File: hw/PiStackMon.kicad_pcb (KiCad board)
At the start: 2 copper layers, 67.5 x 21.5 mm, 61 parts, among them J1 Conn_01x03, J10 Conn_01x02, J2 Conn_01x03, J3 Screw_Terminal_01x02, J4 Screw_Terminal_01x02, J5 Conn_01x02, J6 Conn_01x02, J7 Conn_01x07, J8 Conn_01x05, J9 Conn_01x03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

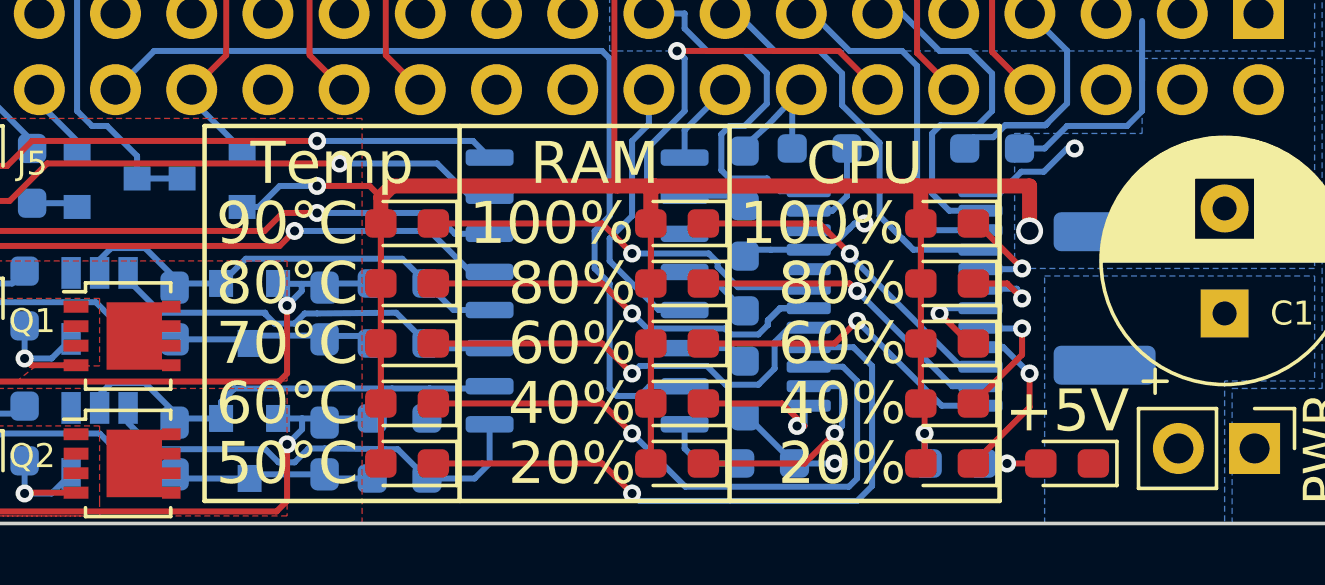
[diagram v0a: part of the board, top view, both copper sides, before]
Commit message: More alt components; JLC assembly component codes
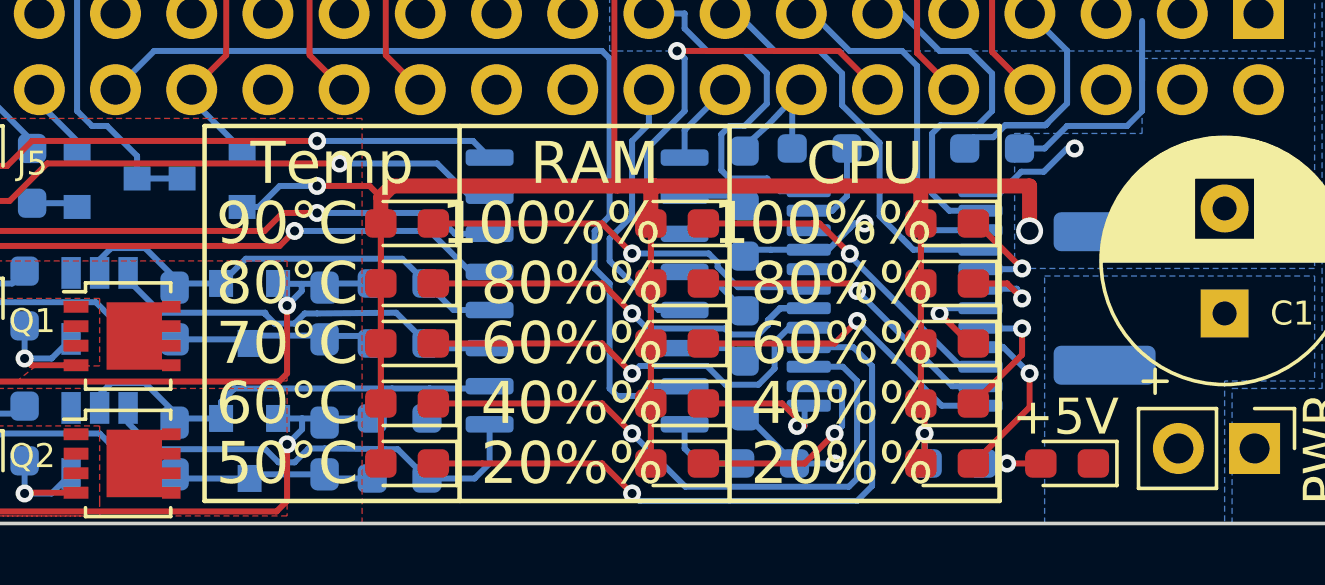
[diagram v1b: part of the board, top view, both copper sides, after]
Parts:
- D1, D6: value 20% -> G
- D10: value 100% -> R
- D11: value 90°C -> R
- D12: value 80°C -> Y
- D13: value 70°C -> G
- D14: value 60°C -> G
- D15: value 50°C -> G
- D16: value +5V -> G
- D2, D7: value 40% -> G
- D3: value 60% -> G
- D4: value 80% -> G
- D5: value 100% -> Y
- D8: value 60% -> Y
- D9: value 80% -> Y
- F1: value MF-MSMF250 -> SMD1812B260TF/12
- R2: value 3k9 -> 7k5
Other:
- board text removed: "+5V"

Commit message: Cleaned up the fabrication data on PCB
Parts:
- moved J8 225.7 mm to (50.1, 27.7)
- moved C1 225.7 mm to (71.8, 40.2)
- moved C2 225.7 mm to (33.3, 28.2)
- moved C3 225.7 mm to (36.8, 40.2)
- moved C4 225.7 mm to (36.8, 44.7)
- moved C5 225.7 mm to (41.8, 40.2)
- moved C6 225.7 mm to (41.8, 44.7)
- moved D1 225.7 mm to (62.5, 45.2)
- moved D10 225.7 mm to (53.5, 37.2)
- moved D11 225.7 mm to (44.5, 37.2)
- moved D12 225.7 mm to (44.5, 39.2)
- moved D13 225.7 mm to (44.5, 41.2)
- moved D14 225.7 mm to (44.5, 43.2)
- moved D15 225.7 mm to (44.5, 45.2)
- moved D16 225.7 mm to (66.5, 45.2)
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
